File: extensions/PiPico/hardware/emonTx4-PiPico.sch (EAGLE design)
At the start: 8 parts, among them U1 RASPBERRY_PICOSMD

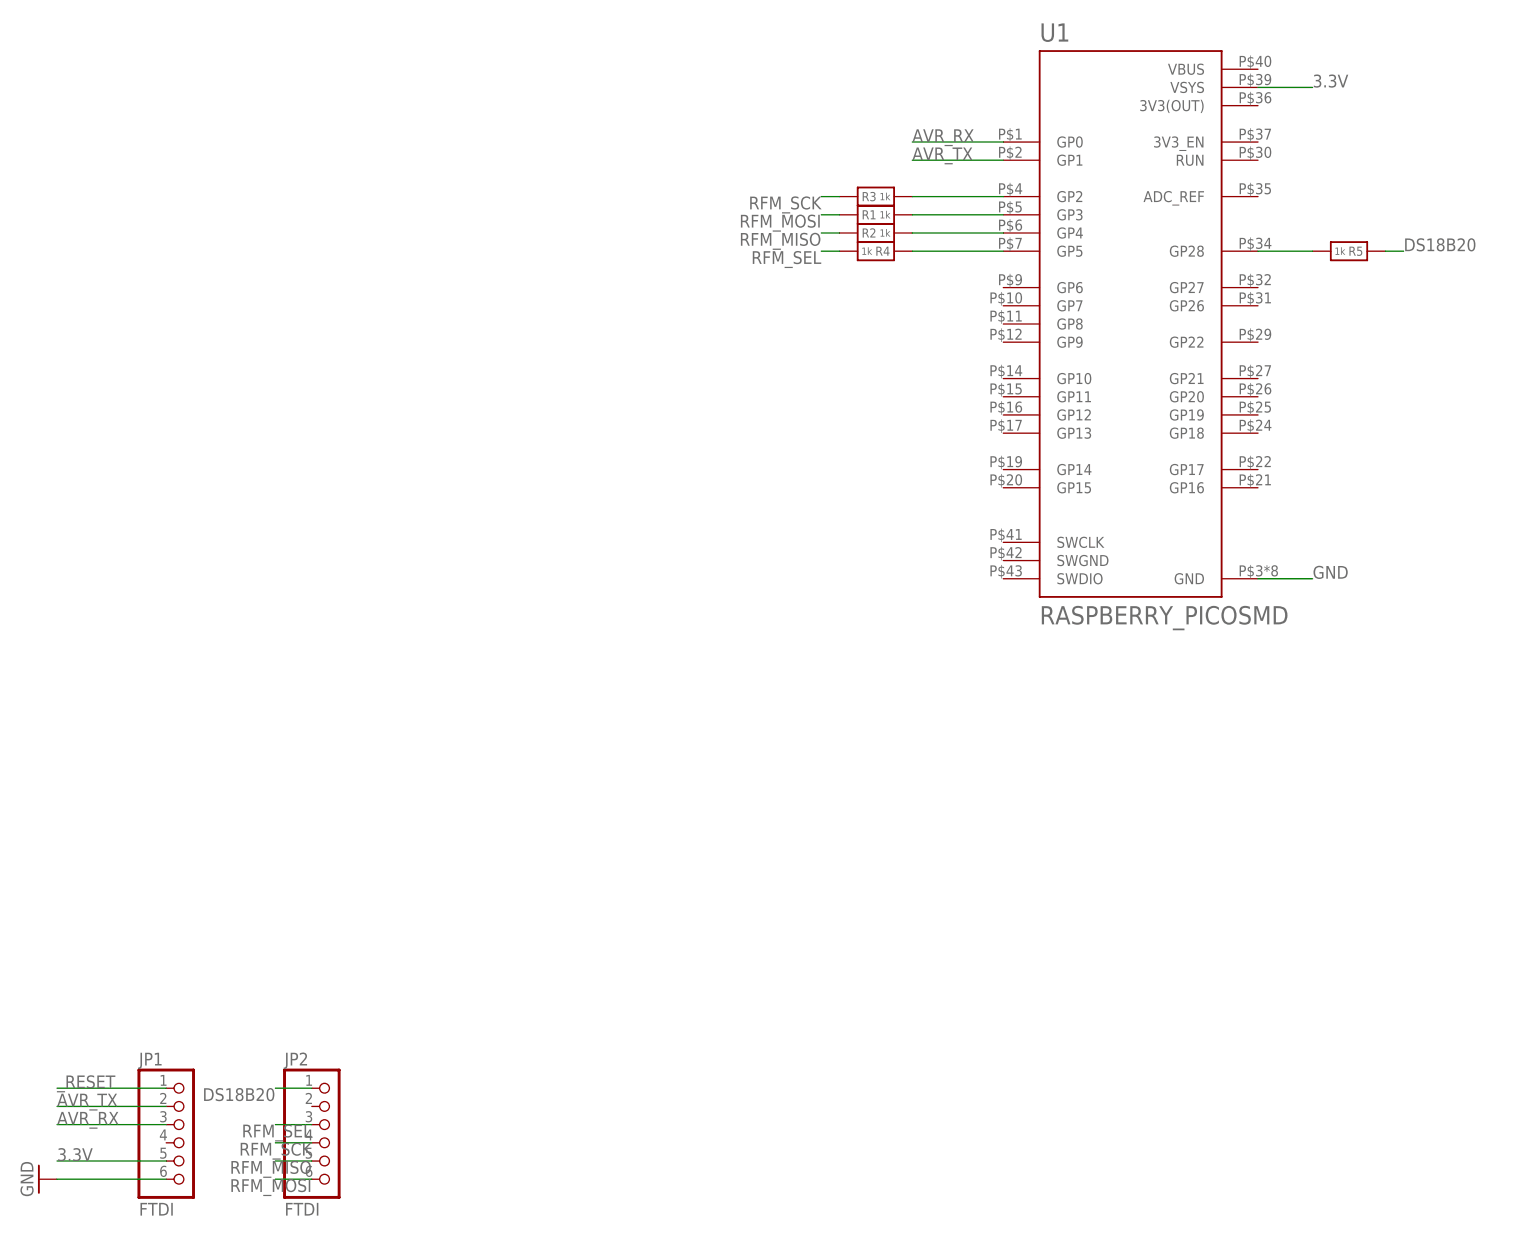
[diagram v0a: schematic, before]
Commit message: updated pi pico extension design
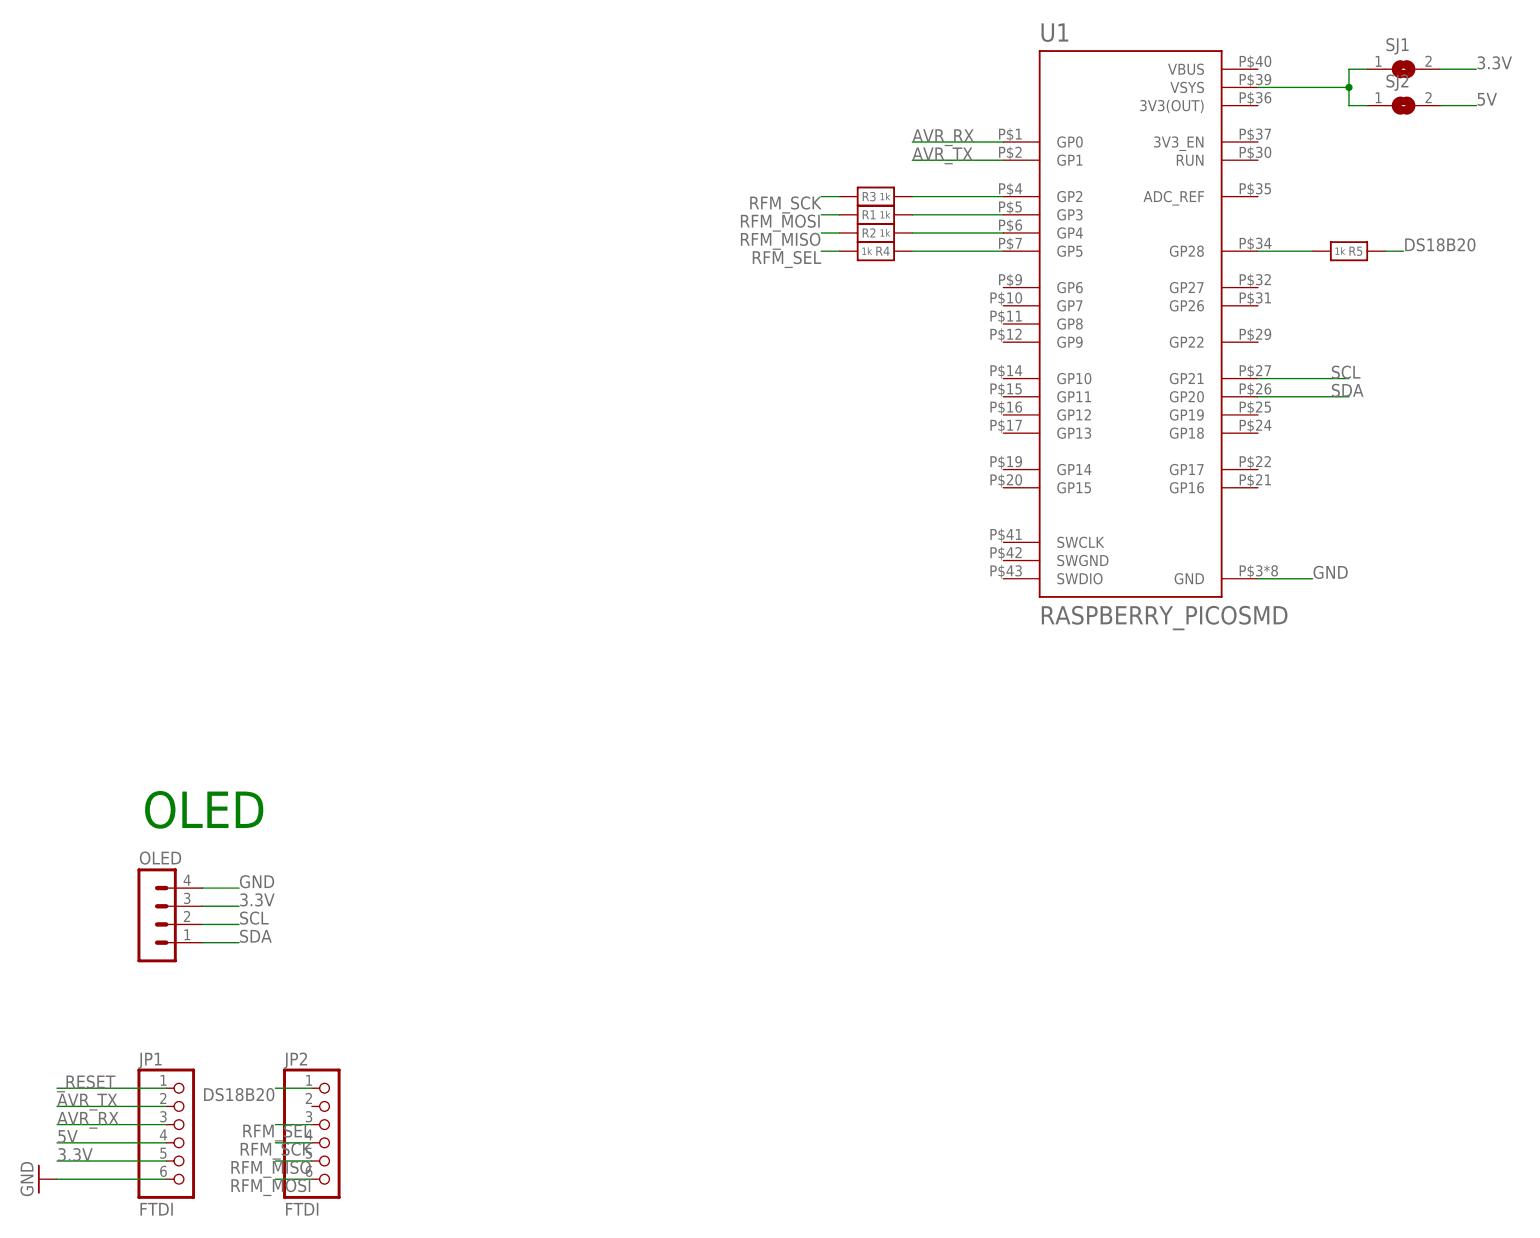
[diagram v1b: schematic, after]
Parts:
- added OLED: (no value), con-lstb-db:MA04-1-OLEDOLED
- added SJ1, SJ2: (no value), jumper:SJ
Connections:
- new net 5V: JP1.4, SJ2.2
- new net N$1: SJ1.1, SJ2.1, U1.VSYS
- new net SCL: OLED.2, U1.GP21
- new net SDA: OLED.1, U1.GP20
- net 3.3V: now also OLED.3, SJ1.2; no longer U1.VSYS
- net GND: now also OLED.4
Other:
- note added: "OLED"
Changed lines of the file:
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@@
 <part name="R1" library="microbuilder" deviceset="RESISTOR" device="_0603" value="1k"/>
 <part name="U1" library="RpiPico" deviceset="RASPBERRY_PICO" device="SMD"/>
+<part name="SJ1" library="jumper" library_urn="urn:adsk.eagle:library:252" deviceset="SJ" device="" package3d_urn="urn:adsk.eagle:package:15471/1"/>
+<part name="SJ2" library="jumper" library_urn="urn:adsk.eagle:library:252" deviceset="SJ" device="" package3d_urn="urn:adsk.eagle:package:15471/1"/>
+<part name="OLED" library="con-lstb-db" deviceset="MA04-1-OLED" device="OLED"/>
 </parts>
 <sheets>
 <sheet>
 <plain>
+<text x="95.758" y="92.202" size="5.08" layer="91" ratio="13">OLED</text>
 </plain>
 <instances>
@@
 <attribute name="NAME" x="220.9645" y="201.9746" size="2.54388125" layer="95"/>
 <attribute name="VALUE" x="220.9731" y="120.6286" size="2.54171875" layer="96"/>
+</instance>
+<instance part="SJ1" gate="1" x="271.78" y="198.12" smashed="yes">
+<attribute name="NAME" x="269.24" y="200.66" size="1.778" layer="95"/>
+<attribute name="VALUE" x="269.24" y="194.31" size="1.778" layer="96"/>
+</instance>
+<instance part="SJ2" gate="1" x="271.78" y="193.04" smashed="yes">
+<attribute name="NAME" x="269.24" y="195.58" size="1.778" layer="95"/>
+<attribute name="VALUE" x="269.24" y="189.23" size="1.778" layer="96"/>
+</instance>
+<instance part="OLED" gate="1" x="96.52" y="81.28" smashed="yes">
+<attribute name="VALUE" x="95.25" y="71.12" size="1.778" layer="96"/>
+<attribute name="NAME" x="95.25" y="87.122" size="1.778" layer="95"/>
 </instance>
 </instances>
@@
 <label x="259.08" y="127" size="1.778" layer="95"/>
 </segment>
+<segment>
+<pinref part="OLED" gate="1" pin="4"/>
+<wire x1="104.14" y1="83.82" x2="109.22" y2="83.82" width="0.1524" layer="91"/>
+<label x="109.22" y="83.82" size="1.778" layer="95"/>
+</segment>
 </net>
 <net name="3.3V" class="0">
@@
 </segment>
 <segment>
-<pinref part="U1" gate="U$1" pin="VSYS"/>
-<wire x1="251.46" y1="195.58" x2="259.08" y2="195.58" width="0.1524" layer="91"/>
-<label x="259.08" y="195.58" size="1.778" layer="95"/>
+<pinref part="SJ1" gate="1" pin="2"/>
+<wire x1="276.86" y1="198.12" x2="281.94" y2="198.12" width="0.1524" layer="91"/>
+<label x="281.94" y="198.12" size="1.778" layer="95"/>
+</segment>
+<segment>
+<pinref part="OLED" gate="1" pin="3"/>
+<wire x1="104.14" y1="81.28" x2="109.22" y2="81.28" width="0.1524" layer="91"/>
+<label x="109.22" y="81.28" size="1.778" layer="95"/>
 </segment>
 </net>
@@
 <wire x1="251.46" y1="172.72" x2="259.08" y2="172.72" width="0.1524" layer="91"/>
 <pinref part="R5" gate="G$1" pin="1"/>
+</segment>
+</net>
+<net name="N$1" class="0">
+<segment>
+<pinref part="U1" gate="U$1" pin="VSYS"/>
+<wire x1="251.46" y1="195.58" x2="264.16" y2="195.58" width="0.1524" layer="91"/>
+<wire x1="264.16" y1="195.58" x2="264.16" y2="198.12" width="0.1524" layer="91"/>
+<wire x1="264.16" y1="198.12" x2="266.7" y2="198.12" width="0.1524" layer="91"/>
+<wire x1="264.16" y1="195.58" x2="264.16" y2="193.04" width="0.1524" layer="91"/>
+<junction x="264.16" y="195.58"/>
+<wire x1="264.16" y1="193.04" x2="266.7" y2="193.04" width="0.1524" layer="91"/>
+<pinref part="SJ1" gate="1" pin="1"/>
+<pinref part="SJ2" gate="1" pin="1"/>
+</segment>
+</net>
+<net name="5V" class="0">
+<segment>
+<pinref part="SJ2" gate="1" pin="2"/>
+<wire x1="276.86" y1="193.04" x2="281.94" y2="193.04" width="0.1524" layer="91"/>
+<label x="281.94" y="193.04" size="1.778" layer="95"/>
+</segment>
+<segment>
+<pinref part="JP1" gate="A" pin="4"/>
+<wire x1="99.06" y1="48.26" x2="83.82" y2="48.26" width="0.1524" layer="91"/>
+<label x="83.82" y="48.26" size="1.778" layer="95"/>
+</segment>
+</net>
+<net name="SDA" class="0">
+<segment>
+<pinref part="OLED" gate="1" pin="1"/>
+<wire x1="104.14" y1="76.2" x2="109.22" y2="76.2" width="0.1524" layer="91"/>
+<label x="109.22" y="76.2" size="1.778" layer="95"/>
+</segment>
+<segment>
+<pinref part="U1" gate="U$1" pin="GP20"/>
+<wire x1="251.46" y1="152.4" x2="264.16" y2="152.4" width="0.1524" layer="91"/>
+<label x="261.62" y="152.4" size="1.778" layer="95"/>
+</segment>
+</net>
+<net name="SCL" class="0">
+<segment>
+<pinref part="OLED" gate="1" pin="2"/>
+<wire x1="104.14" y1="78.74" x2="109.22" y2="78.74" width="0.1524" layer="91"/>
+<label x="109.22" y="78.74" size="1.778" layer="95"/>
+</segment>
+<segment>
+<pinref part="U1" gate="U$1" pin="GP21"/>
+<wire x1="251.46" y1="154.94" x2="264.16" y2="154.94" width="0.1524" layer="91"/>
+<label x="261.62" y="154.94" size="1.778" layer="95"/>
 </segment>
 </net>
@@
 </schematic>
 </drawing>
+<compatibility>
+<note version="8.2" severity="warning">
+Since Version 8.2, EAGLE supports online libraries. The ids
+of those online libraries will not be understood (or retained)
+with this version.
+</note>
+<note version="8.3" severity="warning">
+Since Version 8.3, EAGLE supports URNs for individual library
+assets (packages, symbols, and devices). The URNs of those assets
+will not be understood (or retained) with this version.
+</note>
+<note version="8.3" severity="warning">
+Since Version 8.3, EAGLE supports the association of 3D packages
+with devices in libraries, schematics, and board files. Those 3D
+packages will not be understood (or retained) with this version.
+</note>
+</compatibility>
 </eagle>
